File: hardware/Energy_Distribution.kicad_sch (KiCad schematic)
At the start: 23 parts, among them J15 53398-0271, J16 53398-0671, J17 53398-0671, J18 53398-0271, U17 NVTFS5116PLTAG, U18 NVTFS5116PLTAG, U19 INA199C3DCKR, U21 LMV321RIYLT, U39 NVTFS5116PLTAG, U40 NVTFS5116PLTAG

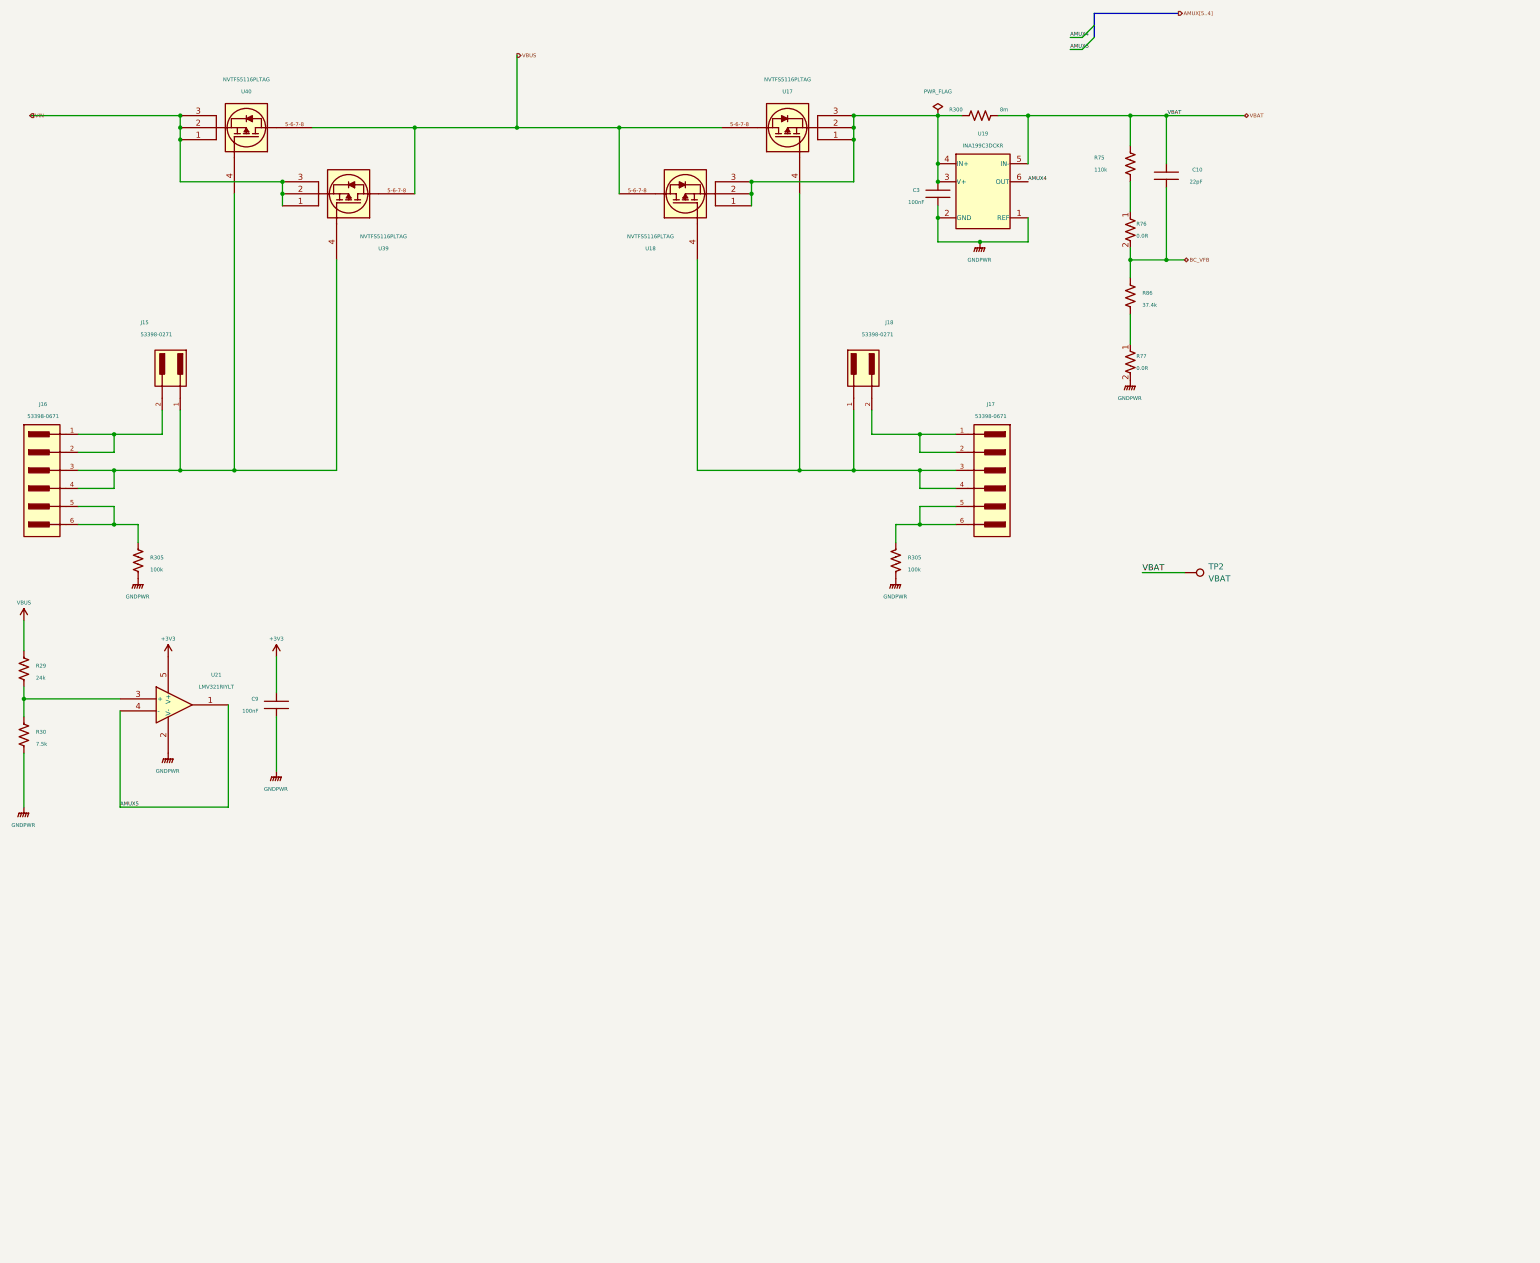
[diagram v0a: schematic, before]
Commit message: hardware: Improving the readability of schematics
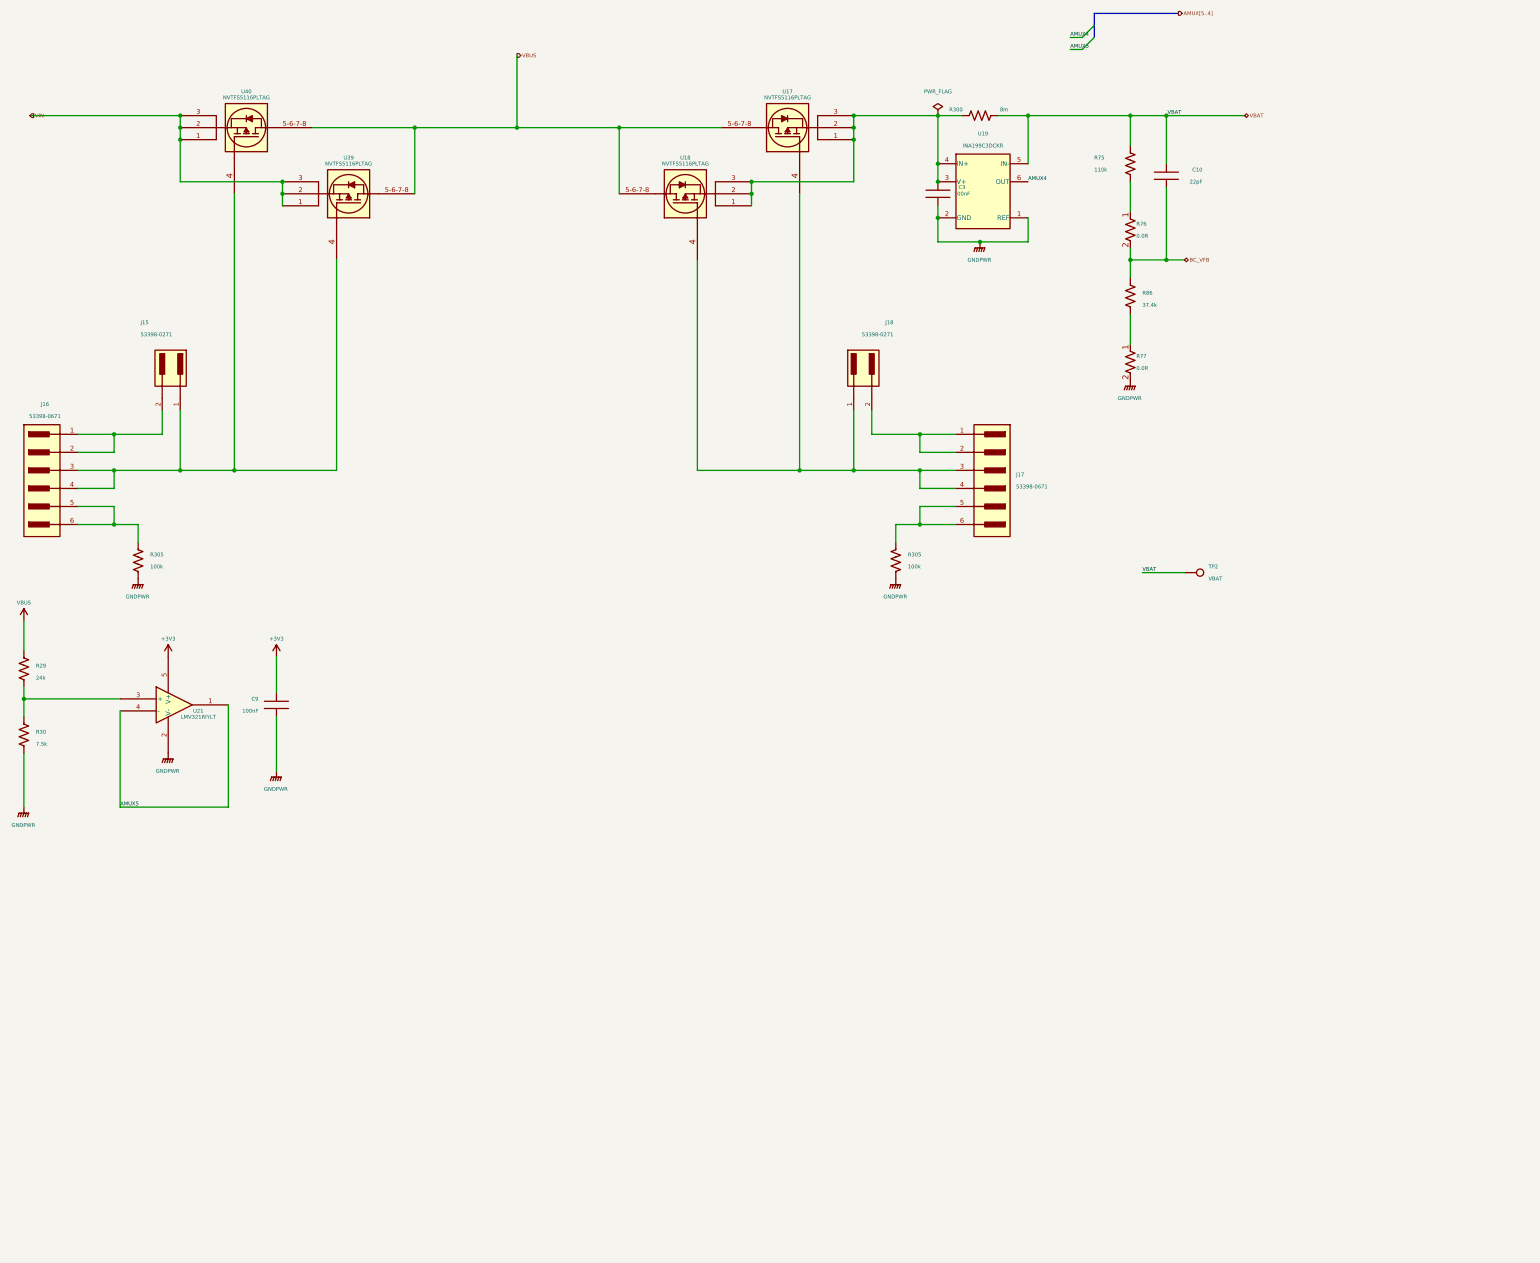
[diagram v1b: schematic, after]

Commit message: hardware: Improving the readability of schematic
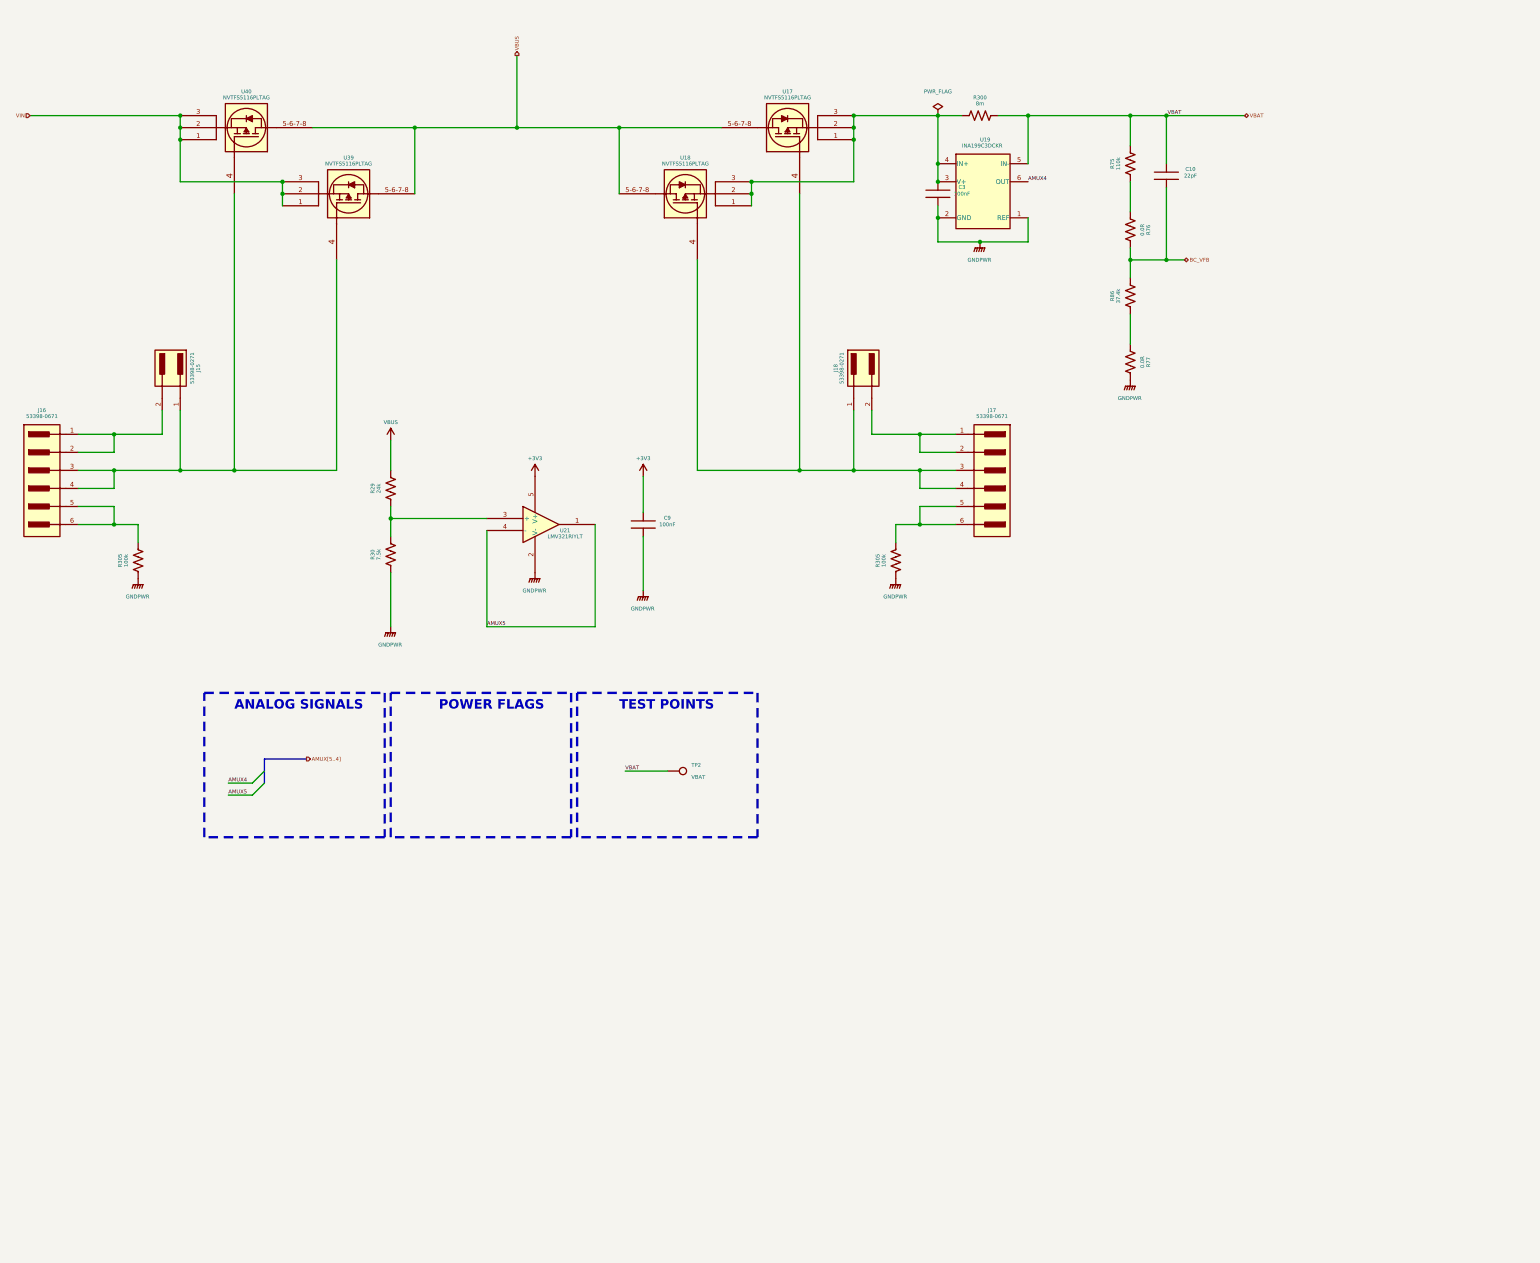
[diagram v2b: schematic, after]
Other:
- note added: "ANALOG SIGNALS"
- note added: "POWER FLAGS"
- note added: "TEST POINTS"
- moved on the sheet: C9, R29, R30, TP2, U21

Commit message: hardware: Making improvements for first release
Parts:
- C10: MPN (none) -> C0603C220K5RACAUTO; Manufacturer (none) -> KEMET; Package (none) -> SMD 0603; automotive Yes -> (none); automotive grade Grade 1 -> (none); capacitance 22 pF -> (none); category Cap -> (none); device class L1 Passive Components -> (none); device class L2 Capacitors -> (none); device class L3 Ceramic Capacitors -> (none); digikey description Cap Ceramic 22pF 50V X7R 10% SMD 0603 125°C Punched Paper T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 -> (none); digikey part number 399-13715-2-ND -> (none); height 0.87mm -> (none); lead free Yes -> (none); library id f369d16140aeee74 -> (none); manufacturer KEMET -> (none); material Ceramic -> (none); mouser description Cap Ceramic 22pF 50V X7R 10% SMD 0603 125°C Punched Paper T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 -> (none); mouser part number 80-C0603C220K5RAUTO -> (none); package 0603 -> (none); rohs Yes -> (none); temperature characteristic X7R -> (none); temperature coefficient 30ppm/°C -> (none); temperature range high +125°C -> (none); temperature range low -55°C -> (none); tolerance 0.1 -> (none); voltage rating 50 V -> (none)
- C3, C9: MPN (none) -> C0603C104K5RACTU; Manufacturer (none) -> KEMET; Package (none) -> SMD 0603; automotive Yes -> (none); automotive grade Grade 1 -> (none); capacitance 0.10 μF -> (none); category Cap -> (none); device class L1 Passive Components -> (none); device class L2 Capacitors -> (none); device class L3 Ceramic Capacitors -> (none); digikey description CAP CER 0.1UF 50V X7R 0603 -> (none); digikey part number 399-5089-2-ND -> (none); height 0.87mm -> (none); lead free Yes -> (none); library id 73022d3323b2b2b8 -> (none); manufacturer KEMET -> (none); material Ceramic -> (none); mouser part number 80-C0603C104K5R7867 -> (none); package 0603 -> (none); rohs Yes -> (none); temperature characteristic X7R -> (none); temperature coefficient 30ppm/°C -> (none); temperature range high +125°C -> (none); temperature range low -55°C -> (none); tolerance 0.1 -> (none); voltage rating 50 V -> (none)
- J16, J17: value 53398-0671 -> 533980671; MPN (none) -> 533980671; Manufacturer (none) -> Molex; Package (none) -> PicoBlade (6P); category Conn -> (none); contact material Tin -> (none); current rating 1A -> (none); device class L1 Connectors -> (none); device class L2 Headers and Wire Housings -> (none); device class L3 unset -> (none); digikey description CONN HEADER 6POS 1.25MM VERT SMD -> (none); digikey part number WM7610CT-ND -> (none); height 4.9mm -> (none); is connector yes -> (none); is male yes -> (none); lead free yes -> (none); library id da45f97994f845ed -> (none); manufacturer Molex -> (none); mouser description Headers & Wire Housings VERTICAL HDR SMT 6P -> (none); mouser part number 538-53398-0671 -> (none); number of contacts 6 -> (none); number of rows 1 -> (none); package HDR6 -> (none); rohs yes -> (none); standoff height 0.05mm -> (none); temperature range high +85°C -> (none); temperature range low -40°C -> (none); voltage rating 125V -> (none)
- R29: symbol CRCW060324K0FKEAHP:RES -> CRCW060324K0FKEAHP:CRCW060324K0FKEAHP; MPN (none) -> CRCW060324K0FKEAHP; Manufacturer (none) -> Vishay; Package (none) -> SMD 0603
- R30: MPN (none) -> CRCW06037K50FKEAHP; Manufacturer (none) -> Vishay; Package (none) -> SMD 0603; automotive Yes -> (none); automotive grade Grade 0 -> (none); category Res -> (none); composition Thick Film -> (none); device class L1 Passive Components -> (none); device class L2 Resistors -> (none); device class L3 Chip SMD Resistors -> (none); height 0.55mm -> (none); ipc land pattern name RESC16085X45 -> (none); lead free Yes -> (none); library id ac0eb7131481e5d0 -> (none); manufacturer Vishay -> (none); package 0603 -> (none); power 250mW -> (none); power rating 0.33W -> (none); resistance 7.5kΩ -> (none); rohs Yes -> (none); series CRCW-HP e3 -> (none); temperature coefficient 100ppm/°C -> (none); temperature range high +155°C -> (none); temperature range low -55°C -> (none); tolerance 1% -> (none); voltage rating 75V -> (none)
- R300: MPN (none) -> WSL20108L000FEA18; Manufacturer (none) -> Vishay; Package (none) -> SMD 2010
- R305: Arrow Part Number CRCW0603100KFKEAHP -> (none); Arrow Price/Stock https://www.arrow.com/en/products/crcw0603100kfkeahp/vishay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 -> (none); Height 0.55 -> (none); MPN (none) -> CRCW0603100KFKEAHP; Manufacturer (none) -> Vishay; Manufacturer_Name Vishay -> (none); Manufacturer_Part_Number CRCW0603100KFKEAHP -> (none); Mouser Part Number 71-CRCW0603100KFKEAH -> (none); Mouser Price/Stock https://www.mouser.co.uk/ProductDetail/Vishay-Dale/CRCW0603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 -> (none); Package (none) -> SMD 0603
- R76, R77: MPN (none) -> CRCW06030000Z0EAHP; Manufacturer (none) -> Vishay; Package (none) -> SMD 0603
- TP2: value VBAT -> Test point; MPN (none) -> N/A; Manufacturer (none) -> N/A; Package (none) -> N/A
- U17, U18, U39, U40: MPN (none) -> NVTFS5116PLTAG; Manufacturer (none) -> onsemi; Package (none) -> WDFN-8
- U19: footprint Package_TO_SOT_SMD:SOT-363_SC-70-6 -> footprints:INA199C3DCKR; symbol INA199C3DCKR:INA199xxDCK -> INA199C3DCKR:INA199C3DCKR; MPN (none) -> INA199C3DCKR; Manufacturer (none) -> TI; Package (none) -> SC70-6
- U21: MPN (none) -> LMV321RIYLT; Manufacturer (none) -> STMicroelectronics; Package (none) -> SOT-23-5
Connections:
- net AMUX4: no longer U19.6 (OUT)
- net GNDPWR: no longer U19.1 (REF)
- net VBAT: no longer U19.5 (IN-)
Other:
- moved on the sheet: U19
